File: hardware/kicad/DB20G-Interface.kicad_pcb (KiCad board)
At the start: 2 copper layers, 65 x 45 mm, 47 parts, among them J1 USB-C, J2 RADIO, J3 HANDSET, J4 DATA, K1 G5V-1-DC5, Q1 2N2222A, Q2 2N2222A, U1 FE1.1s, U2 CP2102N, U3 CM108AH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

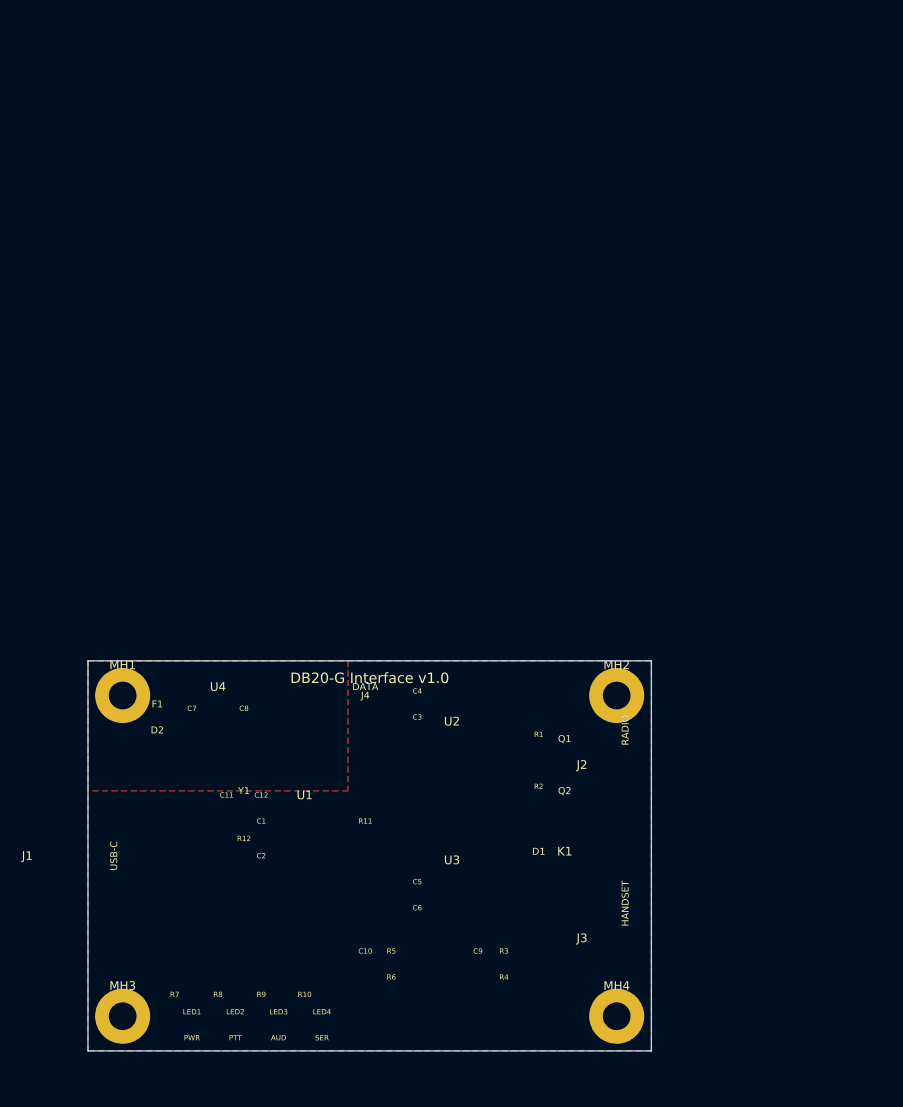
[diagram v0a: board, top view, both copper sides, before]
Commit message: Revision to the Hardware interface
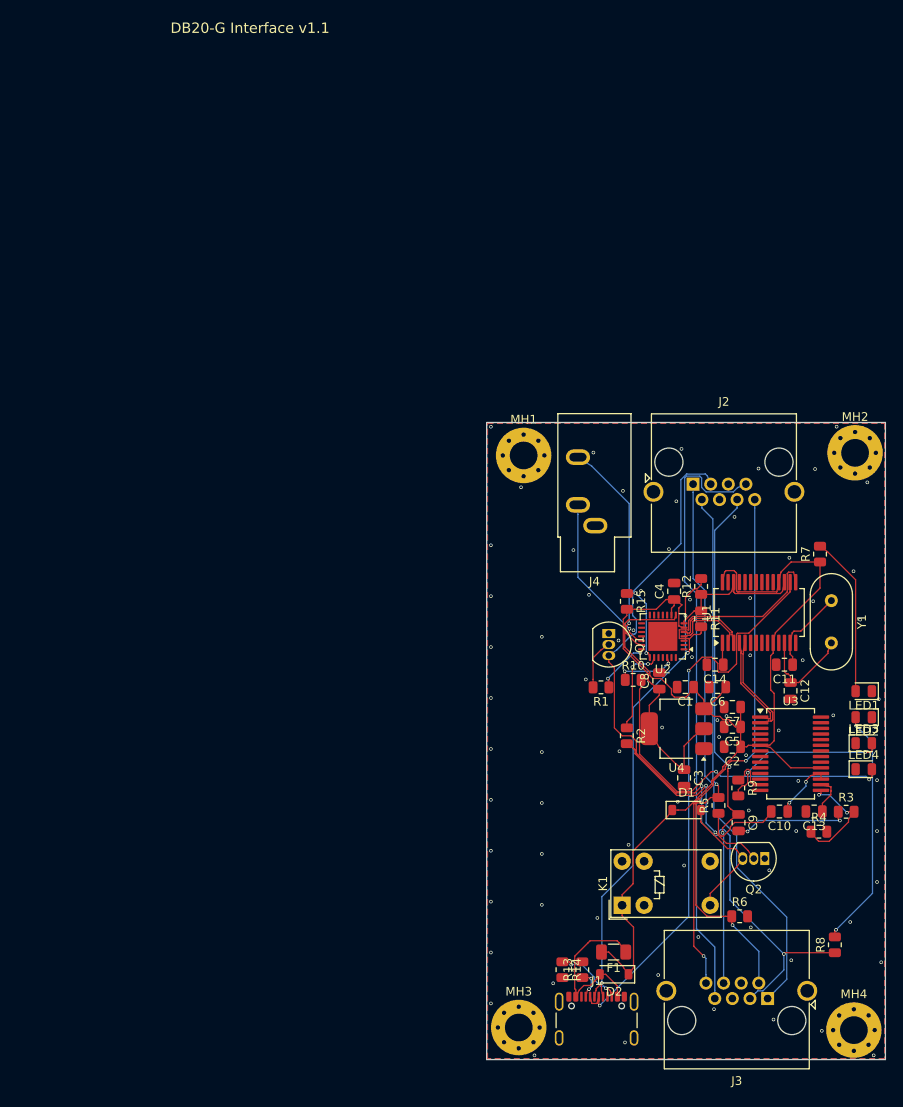
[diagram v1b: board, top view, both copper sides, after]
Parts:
- added C13: 4.7µF, Capacitor_SMD:C_0805_2012Metric, F.Cu at (183.8, 117.4)
- added C14: 100nF, Capacitor_SMD:C_0805_2012Metric, F.Cu at (172.3, 100.4)
- added R13: 5.1kΩ, Resistor_SMD:R_0805_2012Metric, F.Cu at (157.0, 135.6)
- added R14: 5.1kΩ, Resistor_SMD:R_0805_2012Metric, F.Cu at (154.7, 135.6)
- added R15: 10kΩ, Resistor_SMD:R_0805_2012Metric, F.Cu at (162.2, 93.1)
- J1: footprint Connector_USB:USB_C_Receptacle_GCT_USB4105 -> Connector_USB:USB_C_Receptacle_GCT_USB4105-xx-A_16P_TopMnt_Horizontal
- J2, J3: footprint Connector_RJ:RJ45_Amphenol_RJHSE-5380 -> Connector_RJ:RJ45_Amphenol_RJHSE5380
- J4: footprint Connector_Audio:AudioJack_3.5mm_CUI_SJ1-3533NG -> Connector_Audio:Jack_3.5mm_CUI_SJ1-3533NG_Horizontal
- K1: footprint Relay_THT:Relay_DPDT_Omron_G5V-2 -> Relay_THT:Relay_SPDT_Omron_G5V-1
- moved R7 91.0 mm to (184.5, 87.7), turned to 90 degrees
- moved LED1 86.5 mm to (189.5, 103.5), turned to 180 degrees
- moved LED2 80.7 mm to (189.5, 106.5), turned to 180 degrees
- moved LED3 74.9 mm to (189.5, 109.5)
- moved Y1 72.2 mm to (185.8, 93.1), turned to -90 degrees
- moved R8 71.5 mm to (186.2, 132.8), turned to 90 degrees
- moved LED4 69.1 mm to (189.5, 112.5)
- moved C11 66.4 mm to (180.3, 100.4), turned to 180 degrees
- moved C12 62.5 mm to (181.1, 103.5), turned to -90 degrees
- moved C7 62.4 mm to (174.3, 105.3), turned to 180 degrees
- moved J1 62.0 mm to (158.7, 142.4), turned to 0 degrees
- moved R12 61.0 mm to (170.7, 91.4), turned to 90 degrees
- moved R9 60.6 mm to (175.0, 114.7), turned to -90 degrees
- moved U1 59.5 mm to (177.4, 94.4), turned to 90 degrees
- moved F1 59.0 mm to (160.6, 133.6), turned to 180 degrees
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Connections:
- MH1 pad 1: GND -> +3V3
- MH2 pad 1: GND -> +3V3
- MH3 pad 1: GND -> +3V3
- MH4 pad 1: GND -> +3V3
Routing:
- net +3V3: track 0.00 -> 300.0 mm, vias 0 -> 83
- net Net-R2-Q2: track 0.00 -> 104.4 mm, vias 0 -> 5
- net PTT: track 0.00 -> 89.8 mm, vias 0 -> 2
- net /HS_SPKM: track 0.00 -> 70.3 mm
- net /USB_D-: track 0.00 -> 66.7 mm, vias 0 -> 2
- net /HS_VCC: track 0.00 -> 64.7 mm
- net RADIO_MIC: track 0.00 -> 63.4 mm, vias 0 -> 2
- net /HS_UP: track 0.00 -> 60.3 mm, vias 0 -> 2
- net RADIO_SPK: track 0.00 -> 59.2 mm, vias 0 -> 2
- net (no net): track 0.00 -> 44.3 mm, vias 0 -> 2
- net VBUS: track 0.00 -> 19.9 mm
- net RELAY_DRV: track 0.00 -> 14.9 mm
- net /CTS: track 0.00 -> 14.0 mm, vias 0 -> 2
- net Net-C9-R3: track 0.00 -> 13.3 mm, vias 0 -> 2
- net CM108_MIC: track 0.00 -> 12.8 mm, vias 0 -> 2
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- added copper zone on B.Cu, net +3V3
- added copper zone on F.Cu, net +3V3
- removed copper zone on F.Cu, net +5V
- removed copper zone on B.Cu, net GND
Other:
- board size 65 x 45 mm -> 46 x 73.5 mm
- rule pad_to_mask_clearance: 0.051 -> 0
- board text added: "DB20-G Interface v1.1"
- board text removed: "AUD"
- board text removed: "DATA"
- board text removed: "DB20-G Interface v1.0"
- board text removed: "HANDSET"
- board text removed: "PTT"
- board text removed: "PWR"
- board text removed: "RADIO"
- board text removed: "SER"
- board text removed: "USB-C"
